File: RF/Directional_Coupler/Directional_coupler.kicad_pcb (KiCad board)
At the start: 2 copper layers, 60 x 67.5 mm, 59 parts, among them J1 RF in, J2 RF out, J3 Singal, T1 30T, T2 1T, U1 LMH6609MF, U2 LMV358, U3 AD8307, U4 AD8307, U5 LMH6609MF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

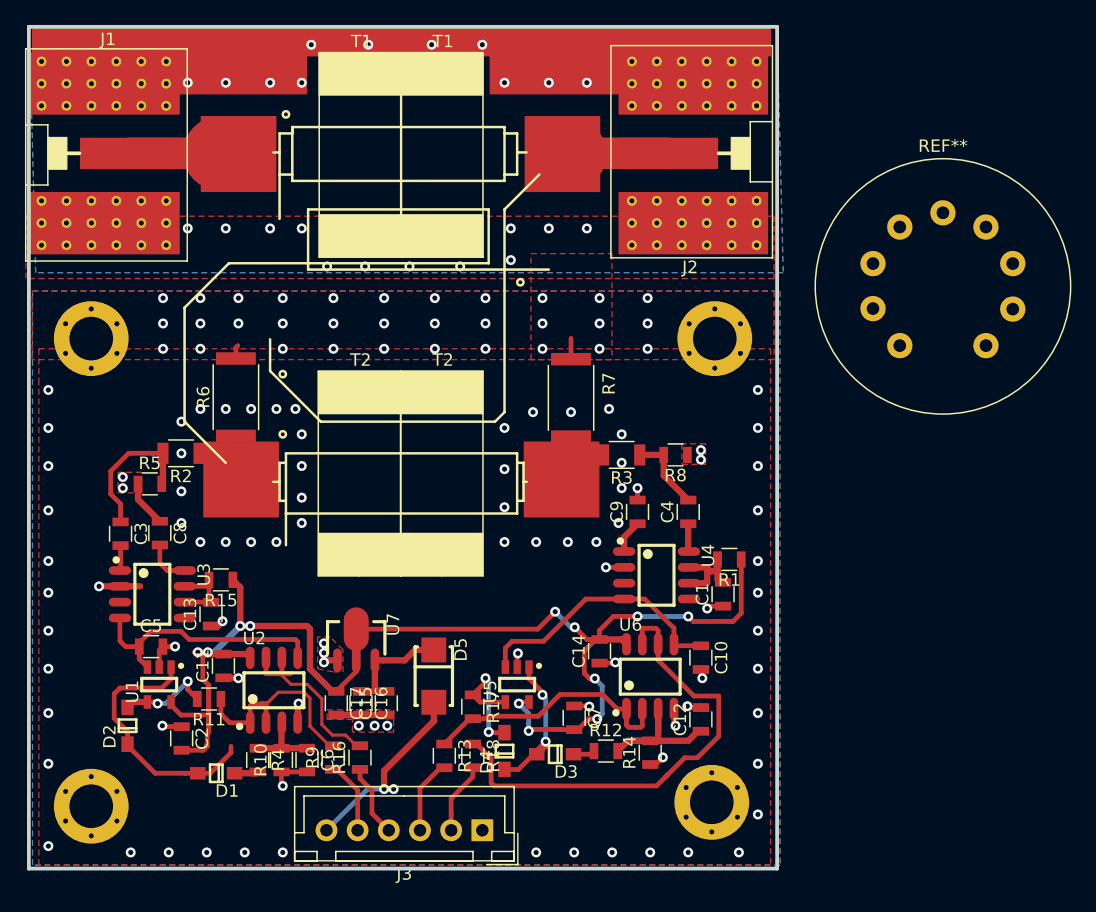
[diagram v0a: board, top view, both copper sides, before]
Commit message: Controller Circuit Done. Now routing
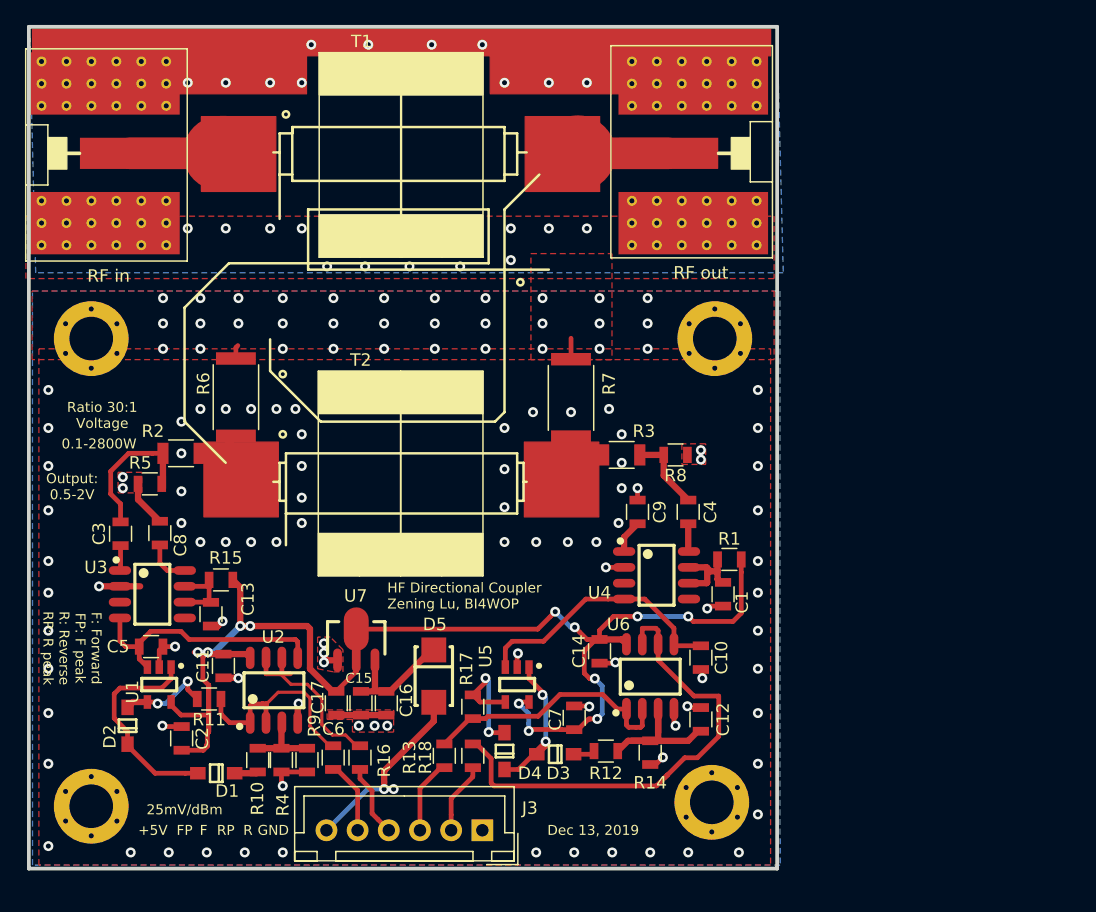
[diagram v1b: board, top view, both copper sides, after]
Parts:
- removed REF**: VALVE-ECC-83-1, Valves:VALVE-ECC-83-1
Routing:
- net Net-(D1-Pad1): track 21.0 -> 17.1 mm
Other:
- board text added: "+5V"
- board text added: "0.1-2800W"
- board text added: "25mV/dBm"
- board text added: "Dec 13, 2019"
- board text added: "F"
- board text added: "F: Forward FP: F peak R: Reverse RP: R peak"
- board text added: "FP"
- board text added: "GND"
- board text added: "HF Directional Coupler Zening Lu, BI4WOP"
- board text added: "Output: 0.5-2V"
- board text added: "R"
- board text added: "RF in"
- board text added: "RF out"
- board text added: "RP"
- board text added: "Ratio 30:1 Voltage"
